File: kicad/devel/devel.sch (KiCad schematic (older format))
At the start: 45 parts, among them J1 CONN_PWR, J2 CONN_X1, J3 CONN_Y2, J4 CONN_X2, J5 CONN_Y1, U1 LM317_SOT223, U2 LM337_SOT223, U3 REF5010IDGK, U4 OPA4197

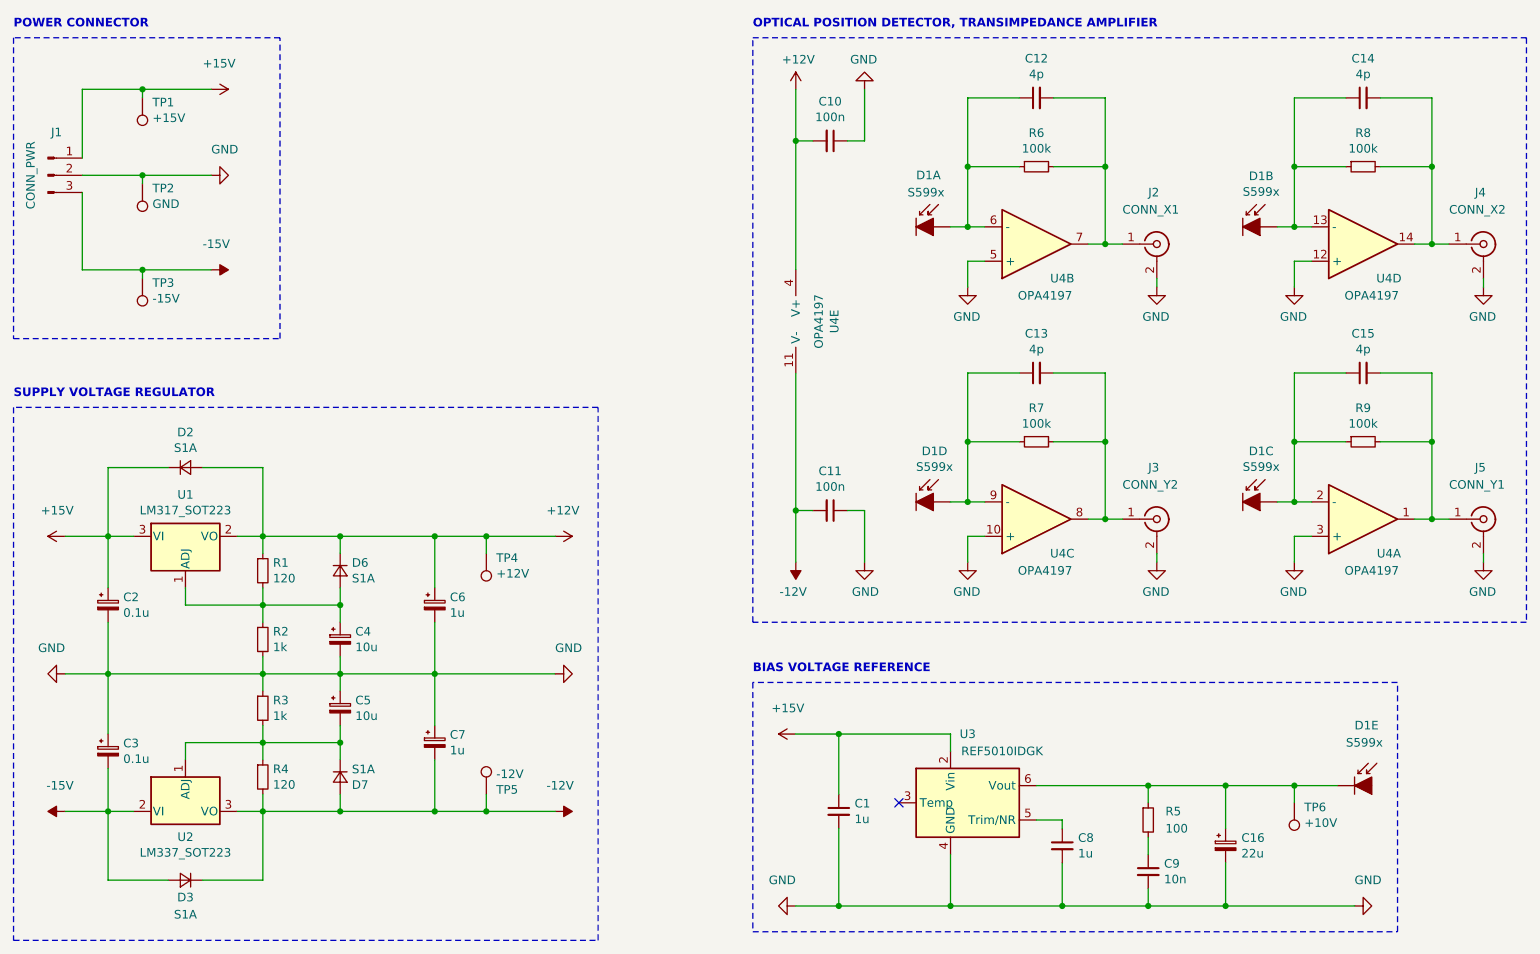
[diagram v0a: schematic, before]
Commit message: started modular PCB design
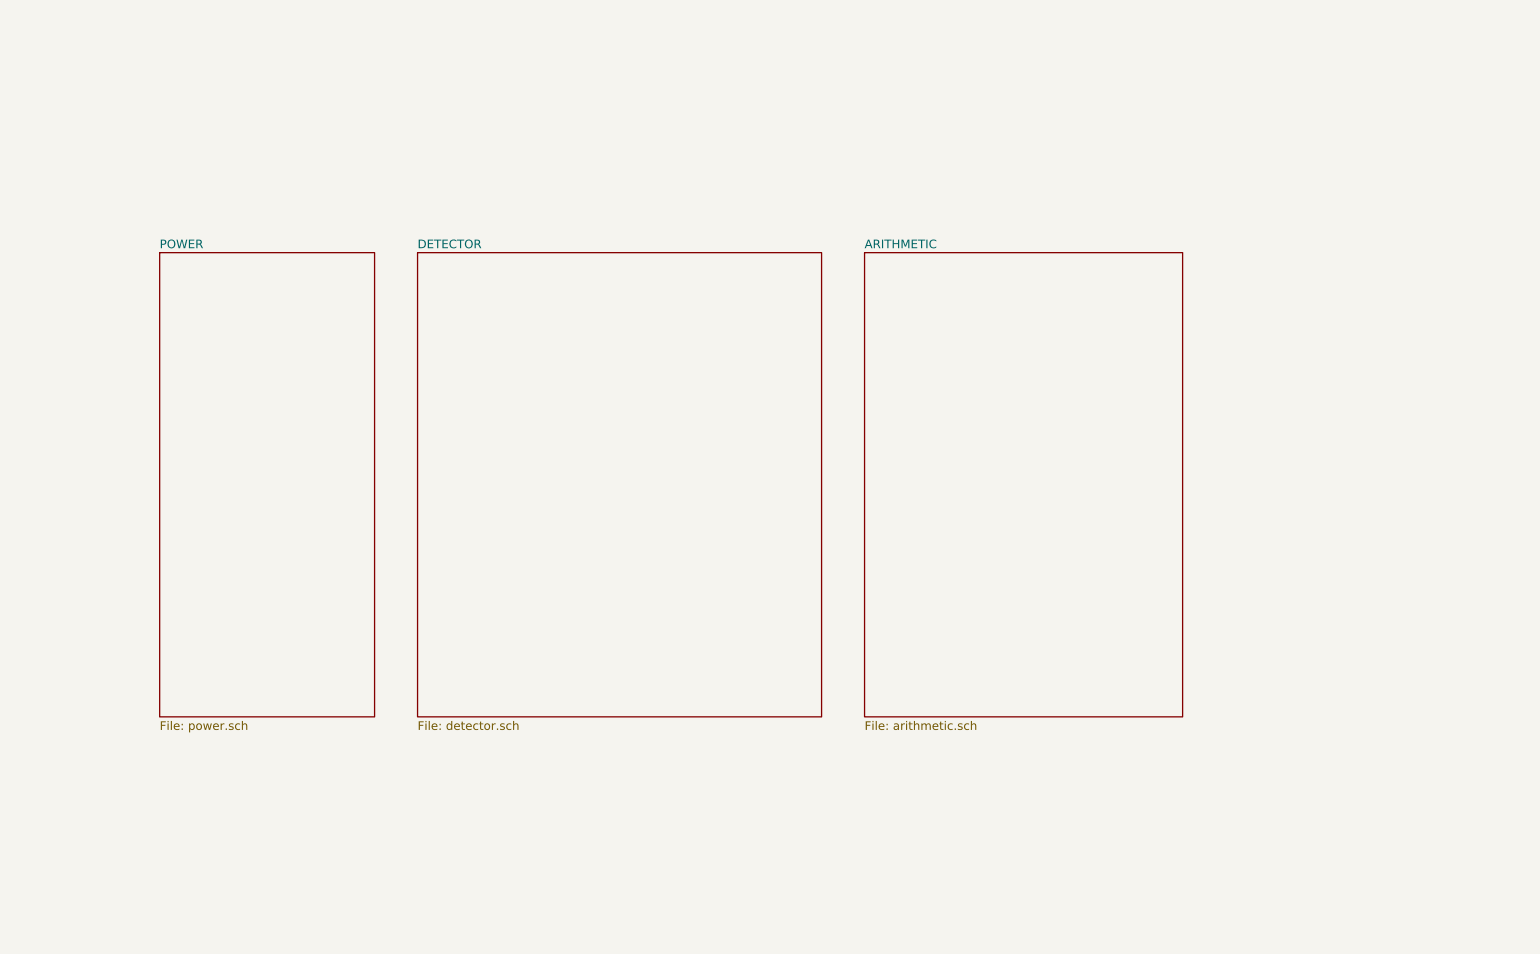
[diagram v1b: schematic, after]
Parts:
- removed C1, C8: 1u, Capacitor_SMD:C_0805_2012Metric, symbol Device:C_Small
- removed C10, C11: 100n, Capacitor_SMD:C_0402_1005Metric, symbol Device:C_Small
- removed C12, C13, C14, C15: 4p, Capacitor_SMD:C_0402_1005Metric, symbol Device:C_Small
- removed C16: 22u, Capacitor_SMD:CP_Elec_5x5.3, symbol Device:CP_Small
- removed C2, C3: 0.1u, Capacitor_SMD:CP_Elec_4x5.4, symbol Device:CP_Small
- removed C4, C5: 10u, Capacitor_SMD:CP_Elec_4x3.9, symbol Device:CP_Small
- removed C6, C7: 1u, Capacitor_SMD:CP_Elec_4x3.9, symbol Device:CP_Small
- removed C9: 10n, Capacitor_SMD:C_0805_2012Metric, symbol Device:C_Small
- removed D1: S599x, Sensor_OpticalPosition:S5990, symbol Sensor_OpticalPosition:S599x
- removed D2, D3, D6, D7: S1A, Diode_SMD:D_SMA, symbol Device:D_Small
- removed J1: CONN_PWR, Connector_PinHeader_2.54mm:PinHeader_1x03_P2.54mm_Vertical_SMD_Pin1Left, symbol Connector:Conn_01x03_Male
- removed J2: CONN_X1, Connector_Coaxial_SMA:SMA_Molex_73251-2120_EdgeMount, symbol Connector:Conn_Coaxial
- removed J3: CONN_Y2, Connector_Coaxial_SMA:SMA_Molex_73251-2120_EdgeMount, symbol Connector:Conn_Coaxial
- removed J4: CONN_X2, Connector_Coaxial_SMA:SMA_Molex_73251-2120_EdgeMount, symbol Connector:Conn_Coaxial
- removed J5: CONN_Y1, Connector_Coaxial_SMA:SMA_Molex_73251-2120_EdgeMount, symbol Connector:Conn_Coaxial
- removed R1, R4: 120, Resistor_SMD:R_0805_2012Metric, symbol Device:R_Small
- removed R2, R3: 1k, Resistor_SMD:R_0805_2012Metric, symbol Device:R_Small
- removed R5: 100, Resistor_SMD:R_0805_2012Metric, symbol Device:R_Small
- removed R6, R7, R8, R9: 100k, Resistor_SMD:R_0805_2012Metric, symbol Device:R_Small
- removed TP1: +15V, TestPoint:TestPoint_Pad_D1.0mm, symbol Connector:TestPoint
- removed TP2: GND, TestPoint:TestPoint_Pad_D1.0mm, symbol Connector:TestPoint
- removed TP3: -15V, TestPoint:TestPoint_Pad_D1.0mm, symbol Connector:TestPoint
- removed TP4: +12V, TestPoint:TestPoint_Pad_D1.0mm, symbol Connector:TestPoint
- removed TP5: -12V, TestPoint:TestPoint_Pad_D1.0mm, symbol Connector:TestPoint
- removed TP6: +10V, TestPoint:TestPoint_Pad_D1.0mm, symbol Connector:TestPoint
- removed U1: LM317_SOT223, Package_TO_SOT_SMD:SOT-223-3_TabPin2, symbol Regulator_Linear:LM317_3PinPackage
- removed U2: LM337_SOT223, Package_TO_SOT_SMD:SOT-223-3_TabPin2, symbol Regulator_Linear:LM337_SOT223
- removed U3: REF5010IDGK, Package_SO:SOIC-8_3.9x4.9mm_P1.27mm, symbol Reference_Voltage:REF5010IDGK
- removed U4: OPA4197, Package_SO:TSSOP-14_4.4x5mm_P0.65mm, symbol Device:Opamp_Quad_Generic
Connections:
- no-connect marks 1 -> 0
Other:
- note removed: "BIAS VOLTAGE REFERENCE"
- note removed: "OPTICAL POSITION DETECTOR, TRANSIMPEDANCE AMPLIFIER"
- note removed: "POWER CONNECTOR"
- note removed: "SUPPLY VOLTAGE REGULATOR"
